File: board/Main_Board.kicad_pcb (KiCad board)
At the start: 2 copper layers, 5 parts, among them U1 Teensy4.1_DEV-16771

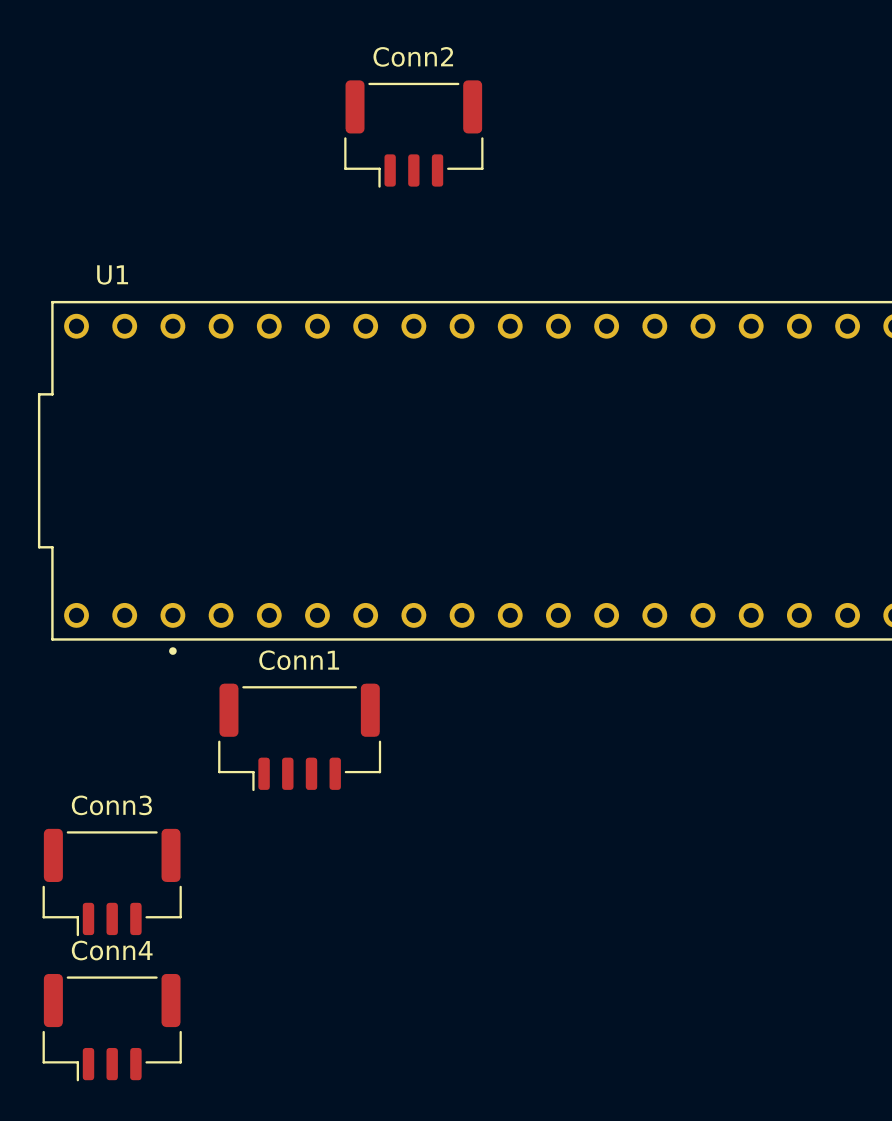
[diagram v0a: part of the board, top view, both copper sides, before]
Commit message: Move Power Indicators
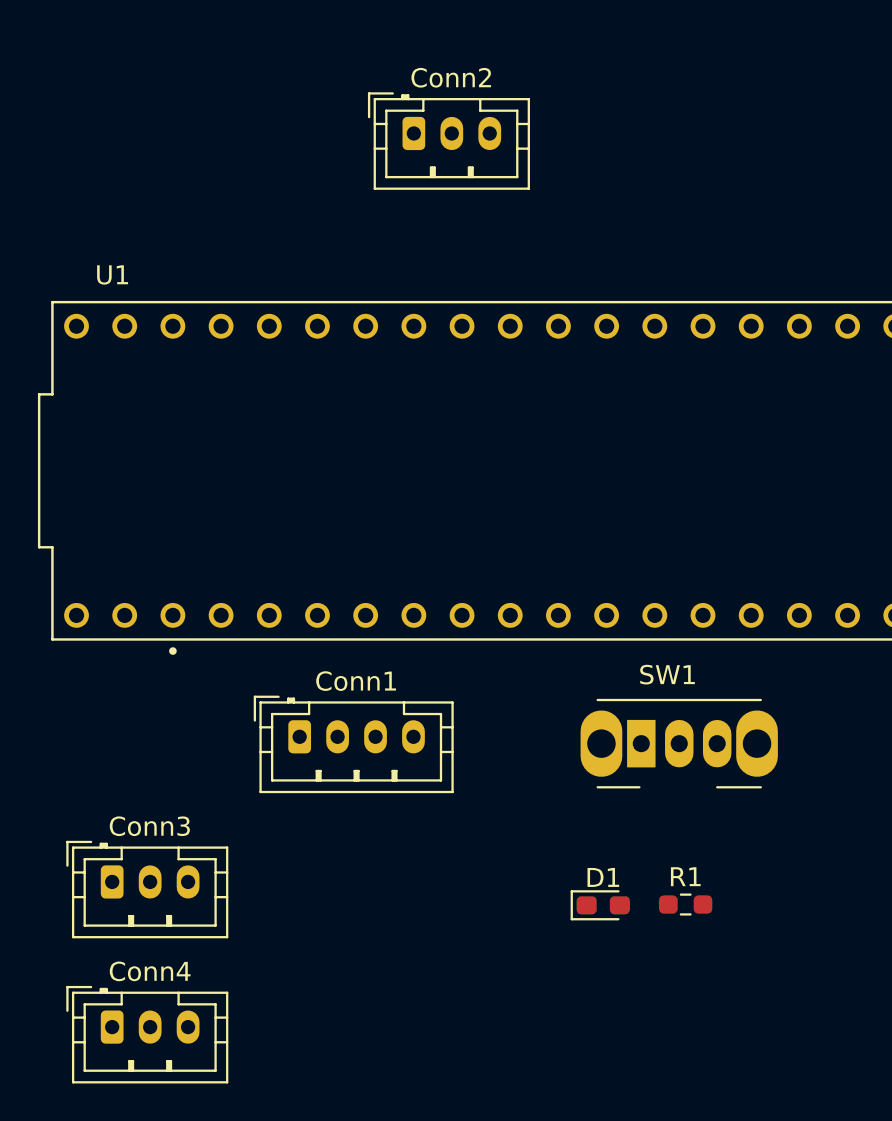
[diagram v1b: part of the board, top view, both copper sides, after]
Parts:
- added D1: LED, LED_SMD:LED_0603_1608Metric_Pad1.05x0.95mm_HandSolder, F.Cu at (144.6, 106.7)
- added R1: 330, Resistor_SMD:R_0603_1608Metric_Pad0.98x0.95mm_HandSolder, F.Cu at (148.9, 106.7)
- added SW1: SW_SPDT, Button_Switch_THT:SW_Slide_SPDT_Angled_CK_OS102011MA1Q, F.Cu at (146.6, 98.2)
- Conn1: footprint Connector_JST:JST_GH_BM04B-GHS-TBT_1x04-1MP_P1.25mm_Vertical -> Connector_JST:JST_PH_B4B-PH-K_1x04_P2.00mm_Vertical
- Conn2, Conn3, Conn4: footprint Connector_JST:JST_GH_BM03B-GHS-TBT_1x03-1MP_P1.25mm_Vertical -> Connector_JST:JST_PH_B3B-PH-K_1x03_P2.00mm_Vertical
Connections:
- U1 pad 19: unconnected-(U1-A5-Pad19) -> Enable

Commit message: Fix Breakout Board
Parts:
- added Conn5: Molex_SL_03, Connector_JST:JST_PH_B3B-PH-K_1x03_P2.00mm_Vertical, F.Cu at (177.9, 68.1)
- moved Conn4 51.8 mm to (145.8, 69.0)
- moved Conn3 51.4 mm to (154.9, 69.1)
- moved D1 45.7 mm to (173.2, 71.1)
- moved R1 41.0 mm to (173.2, 73.7)
- moved SW1 37.6 mm to (122.9, 69.1), turned to 180 degrees
- moved Conn2 29.6 mm to (164.1, 69.1)
- moved Conn1 29.4 mm to (134.7, 69.1)
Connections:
- U1 pad 17: QE1-1 -> AE4
- U1 pad 18: QE1-2 -> QE1-1
- U1 pad 19: Enable -> QE1-2
- U1 pad 20: unconnected-(U1-A6-Pad20) -> Enable
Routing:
- net (no net): track 0.00 -> 168.0 mm
- net AE1: track 0.00 -> 7.13 mm, vias 0 -> 2
- net AE2: track 0.00 -> 3.06 mm
- net Net-(D1-A): track 0.00 -> 2.50 mm

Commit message: Update Mini Arm Board
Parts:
- added Enable: BLUE, LED_SMD:LED_0603_1608Metric_Pad1.05x0.95mm_HandSolder, F.Cu at (116.8, 73.0)
- added R3: 200, Resistor_SMD:R_0603_1608Metric_Pad0.98x0.95mm_HandSolder, F.Cu at (118.7, 73.0)
- Power: renamed from D1; value LED -> GREEN
- moved Conn5 36.1 mm to (141.7, 68.1)
- moved Conn3 5.24 mm to (160.1, 68.1)
- moved Conn2 5.18 mm to (169.2, 68.1)
- moved Conn4 5.14 mm to (150.9, 68.1)
- moved Conn1 4.28 mm to (130.6, 68.1)
- moved R1 3.11 mm to (170.2, 73.0)
- moved Power 2.07 mm to (174.0, 73.0), turned to 180 degrees
- moved OFF 1.94 mm to (123.9, 67.4)
- renumbered SW1 to OFF
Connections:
- net QE1-1 renamed QE1-A
- net QE1-2 renamed QE1-B
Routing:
- net (no net): track 168.0 -> 0.00 mm
- net +3V3: track 0.00 -> 78.0 mm, vias 0 -> 1
- net AE1: track 7.13 -> 29.6 mm, vias 2 -> 0
- net Enable: track 0.00 -> 21.1 mm
- net AE2: track 3.06 -> 23.6 mm
- net AE3: track 0.00 -> 17.3 mm
- net AE4: track 0.00 -> 11.0 mm
- net QE1-A: track 0.00 -> 9.21 mm
- net QE1-B: track 0.00 -> 8.98 mm
- net Net-(D3-A): track 0.00 -> 1.92 mm
- added copper zone on B.Cu, net GND
- added copper zone on F.Cu, net GND
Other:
- board outline added: 64.1 x 30.5 mm
- board text added: "3V3"
- board text added: "GND"
- board text added: "Main Arm Controller Mars Rover Design Team Missouri S&T, 2026 Lucas Boeyink Tyler Hughes"
- board text added: "PWM"
- board text added: "PWM.A"

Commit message: Update Main Board
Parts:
- removed Power: GREEN, LED_SMD:LED_0603_1608Metric_Pad1.05x0.95mm_HandSolder
- removed the R1 at (170.2, 73.0)
- added D1: GREEN, LED_SMD:LED_0603_1608Metric_Pad1.05x0.95mm_HandSolder, F.Cu at (113.5, 67.9)
- added D1: GREEN, LED_SMD:LED_0603_1608Metric_Pad1.05x0.95mm_HandSolder, F.Cu at (92.5, 66.1)
- added H3: MountingHole, MountingHole:MountingHole_4.3mm_M4_ISO14580_Pad_TopBottom, F.Cu at (81.9, 52.7)
- added R1: 330, Resistor_SMD:R_0603_1608Metric_Pad0.98x0.95mm_HandSolder, F.Cu at (96.9, 66.0)
- added R1: 330, Resistor_SMD:R_0603_1608Metric_Pad0.98x0.95mm_HandSolder, F.Cu at (115.6, 67.9)
- moved U1 3.89 mm to (142.2, 84.6)
- moved D3 3.30 mm to (113.5, 72.9)
- moved R3 3.30 mm to (115.4, 72.9)
- moved SW1 2.17 mm to (124.2, 65.2)
- renumbered Enable to D3, OFF to SW1
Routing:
- net +3V3: track 78.0 -> 88.9 mm
- net AE1: track 29.6 -> 34.8 mm
- net AE3: track 17.3 -> 20.8 mm
- net AE4: track 11.0 -> 12.1 mm
- net AE2: track 23.6 -> 24.8 mm
- net Enable: track 21.1 -> 22.1 mm
- net QE1-B: track 8.98 -> 9.61 mm
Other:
- board size 64.1 x 30.5 mm -> 66.7 x 33.7 mm
- board text added: "A PWM"
- board text added: "B PWM"
- board text added: "DATA"
- board text added: "ON"
- board text removed: "PWM.A"

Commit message: Add main board general layout
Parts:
- removed Conn1: Molex_SL_04, Connector_JST:JST_PH_B4B-PH-K_1x04_P2.00mm_Vertical
- removed Conn2, Conn3, Conn4, Conn5: Molex_SL_03, Connector_JST:JST_PH_B3B-PH-K_1x03_P2.00mm_Vertical
- removed the D1 at (113.5, 67.9)
- removed the D1 at (92.5, 66.1)
- removed the R1 at (96.9, 66.0)
- removed the R1 at (115.6, 67.9)
- added C1: 4.7u, Capacitor_SMD:C_0603_1608Metric_Pad1.08x0.95mm_HandSolder, F.Cu at (167.0, 98.4)
- added D1: GREEN, LED_SMD:LED_0603_1608Metric_Pad1.05x0.95mm_HandSolder, F.Cu at (137.1, 68.6)
- added H1: MountingHole, MRDT_Drill_Holes:4_40_Hole, F.Cu at (119.4, 71.9)
- added H2: MountingHole, MRDT_Drill_Holes:4_40_Hole, F.Cu at (172.9, 72.0)
- added H4: MountingHole, MRDT_Drill_Holes:4_40_Hole, F.Cu at (119.4, 98.3)
- added J1: X Axis Encoder, Connector_JST:JST_PH_B4B-PH-K_1x04_P2.00mm_Vertical, F.Cu at (146.6, 69.8)
- added J2: J2 Encoder, Connector_JST:JST_PH_B3B-PH-K_1x03_P2.00mm_Vertical, F.Cu at (161.5, 100.3)
- added J3: J3 Encoder, Connector_JST:JST_PH_B3B-PH-K_1x03_P2.00mm_Vertical, F.Cu at (151.3, 100.3)
- added J4: J4 Encoder, Connector_JST:JST_PH_B3B-PH-K_1x03_P2.00mm_Vertical, F.Cu at (141.2, 100.3)
- added J5: Pitch Encoder, Connector_JST:JST_PH_B3B-PH-K_1x03_P2.00mm_Vertical, F.Cu at (130.8, 100.3)
- added J6: I2C Bus, Connector_JST:JST_PH_B2B-PH-K_1x02_P2.00mm_Vertical, F.Cu at (161.3, 69.8)
- added R1: 330, Resistor_SMD:R_0603_1608Metric_Pad0.98x0.95mm_HandSolder, F.Cu at (137.9, 71.4)
- added R2: 200, Resistor_SMD:R_0603_1608Metric_Pad0.98x0.95mm_HandSolder, F.Cu at (141.8, 71.5)
- added R4: 4.7k, Resistor_SMD:R_0603_1608Metric_Pad0.98x0.95mm_HandSolder, F.Cu at (157.5, 71.1)
- H3: footprint MountingHole:MountingHole_4.3mm_M4_ISO14580_Pad_TopBottom -> MRDT_Drill_Holes:4_40_Hole
- R3: value 200 -> 4.7k
- SW1: value SW_SPDT -> Enable Switch
- moved H3 101.8 mm to (172.9, 98.3)
- moved R3 43.6 mm to (159.0, 74.3), turned to 0 degrees
- moved D3 27.6 mm to (140.8, 68.6), turned to 0 degrees
- moved SW1 8.23 mm to (131.0, 69.8)
- moved U1 3.84 mm to (146.1, 85.1)
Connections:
- R3 pad 1: Net-(D3-A) -> +3V3
- R3 pad 2: Enable -> SDA
- U1 pad 18: QE1-A -> SDA
- U1 pad 19: QE1-B -> SCL
- U1 pad 21: unconnected-(U1-A7-Pad21) -> QE1-A
- U1 pad 22: unconnected-(U1-A8-Pad22) -> QE1-B
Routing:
- net +3V3: track 88.9 -> 46.4 mm, vias 1 -> 3
- net AE1: track 34.8 -> 0.00 mm
- net SDA: track 0.00 -> 30.0 mm, vias 0 -> 1
- net SCL: track 0.00 -> 30.0 mm, vias 0 -> 2
- net AE2: track 24.8 -> 0.00 mm
- net AE3: track 20.8 -> 0.00 mm
- net QE1-B: track 9.61 -> 29.3 mm, vias 0 -> 2
- net QE1-A: track 9.39 -> 25.2 mm, vias 0 -> 2
- net AE4: track 12.1 -> 0.00 mm
- net Enable: track 22.1 -> 20.7 mm
- removed copper zone on B.Cu, net GND
- removed copper zone on F.Cu, net GND
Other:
- board size 66.7 x 33.7 mm -> 61.6 x 34.5 mm
- board text removed: "3V3"
- board text removed: "A PWM"
- board text removed: "B PWM"
- board text removed: "DATA"
- board text removed: "GND"
- board text removed: "Main Arm Controller Mars Rover Design Team Missouri S&T, 2026 Lucas Boeyink Tyler Hughes"
- board text removed: "ON"
- board text removed: "PWM"

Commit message: Complete main board pre-review
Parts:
- I2C Bus: renamed from J6
- J2 Encoder: renamed from J2
- J3 Encoder: renamed from J3
- J4 Encoder: renamed from J4
- Pitch Encoder: renamed from J5
- X Axis Encoder: renamed from J1
- moved R3 0.63 mm to (158.4, 74.3)
- moved H2 0.46 mm to (172.8, 71.5)
- moved H1 0.38 mm to (119.4, 71.5)
- moved H3 0.26 mm to (172.8, 98.6)
- moved H4 0.25 mm to (119.4, 98.6)
- renumbered SW1 to ENABLE
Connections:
- U1 pad 14: AE1 -> unconnected-(U1-A0-Pad14)
- U1 pad 15: AE2 -> unconnected-(U1-A1-Pad15)
- U1 pad 16: AE3 -> unconnected-(U1-A2-Pad16)
- U1 pad 17: AE4 -> unconnected-(U1-A3-Pad17)
- U1 pad 24: unconnected-(U1-A10-Pad24) -> AE4
- U1 pad 25: unconnected-(U1-A11-Pad25) -> AE3
- U1 pad 26: unconnected-(U1-A12-Pad26) -> AE2
- U1 pad 27: unconnected-(U1-A13-Pad27) -> AE1
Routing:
- net +3V3: track 46.4 -> 111.3 mm, vias 3 -> 8
- net AE4: track 0.00 -> 31.8 mm, vias 0 -> 2
- net AE3: track 0.00 -> 25.1 mm, vias 0 -> 2
- net AE2: track 0.00 -> 17.3 mm, vias 0 -> 2
- net AE1: track 0.00 -> 10.0 mm, vias 0 -> 2
- net SCL: track 30.0 -> 32.4 mm
- net Enable: track 20.7 -> 19.1 mm
- net QE1-B: track 29.3 -> 30.5 mm
- net QE1-A: track 25.2 -> 26.1 mm
- added copper zone on B.Cu, net GND
- added copper zone on F.Cu, net GND
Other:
- board size 61.6 x 34.5 mm -> 61.6 x 35.2 mm
- board text added: "3V3"
- board text added: "A"
- board text added: "B"
- board text added: "DISABLE"
- board text added: "ENABLE"
- board text added: "GND"
- board text added: "Mini Arm Controller Main Board Mars Rover Design Team Missouri S&T, 2026 Lucas Boeyink, Tyler Hughes"
- board text added: "OUT"
- board text added: "POWER"
- board text added: "SCL"
- board text added: "SDA"

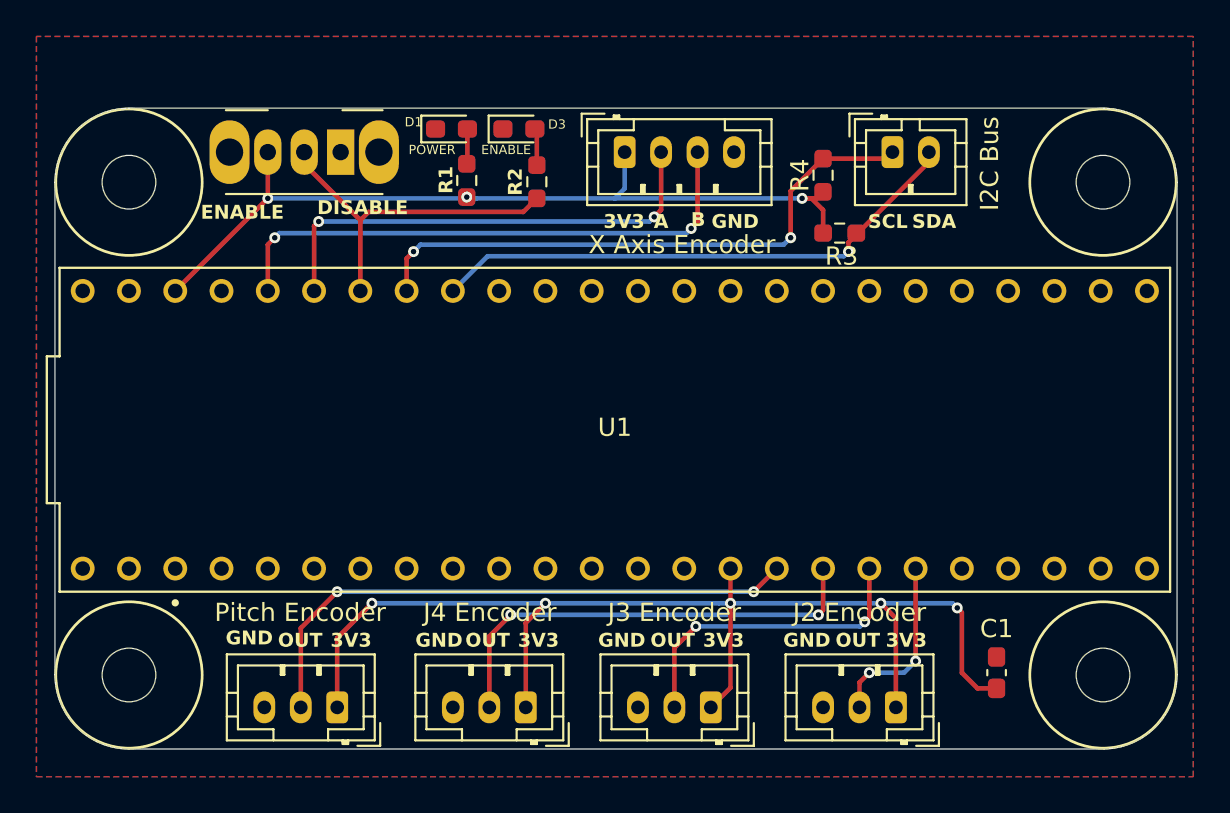
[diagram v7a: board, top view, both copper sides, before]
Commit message: Adjust main board size
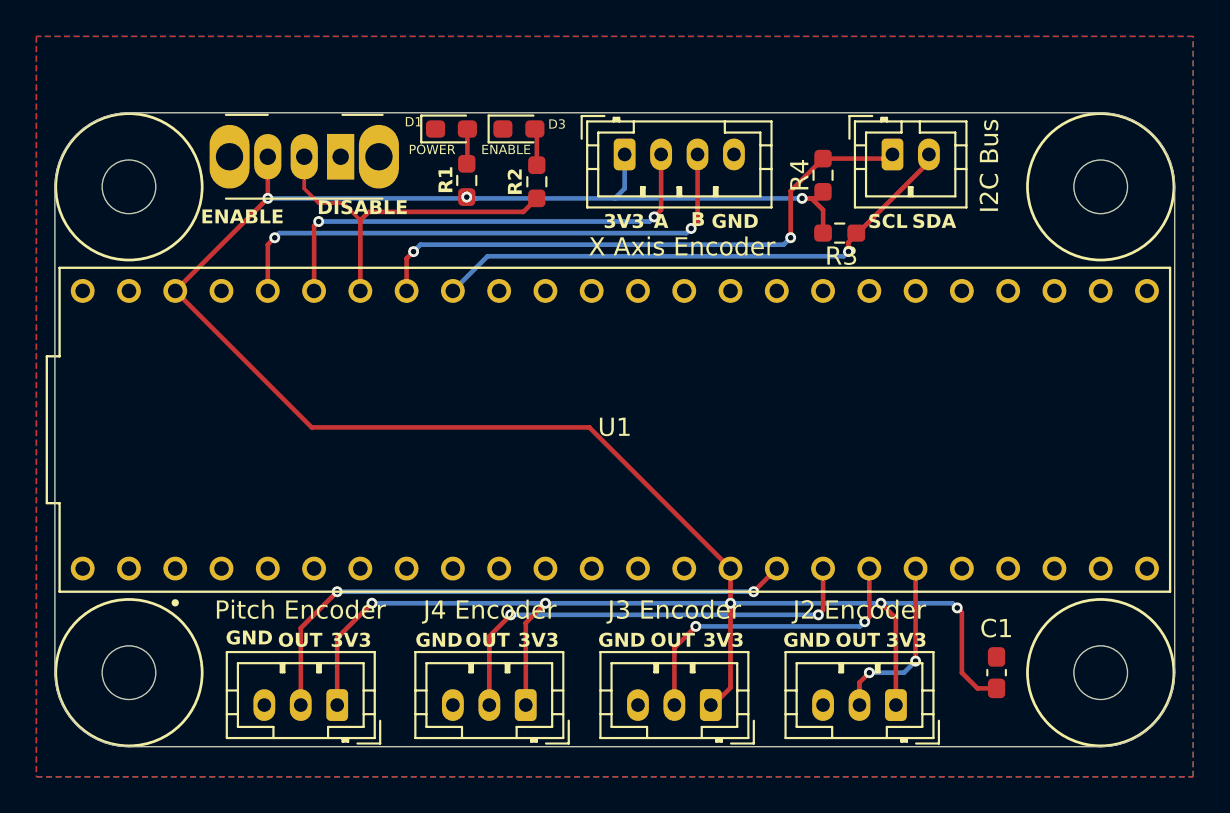
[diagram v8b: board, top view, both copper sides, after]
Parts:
- removed H1, H4: MountingHole, MRDT_Drill_Holes:4_40_Hole
- added H2: MountingHole, MRDT_Drill_Holes:4_40_Hole, F.Cu at (119.4, 71.8)
- added H3: MountingHole, MRDT_Drill_Holes:4_40_Hole, F.Cu at (119.4, 98.4)
- moved H2 0.28 mm to (172.7, 71.8)
- moved ENABLE 0.25 mm to (131.0, 70.1)
- moved H3 0.18 mm to (172.7, 98.4)
- moved I2C Bus 0.13 mm to (161.3, 70.0)
- moved X Axis Encoder 0.13 mm to (146.6, 70.0)
- moved J2 Encoder 0.13 mm to (161.5, 100.2)
- moved J3 Encoder 0.13 mm to (151.3, 100.2)
- moved J4 Encoder 0.13 mm to (141.2, 100.2)
- moved Pitch Encoder 0.13 mm to (130.8, 100.2)
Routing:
- net +3V3: track 111.3 -> 147.8 mm
- net Enable: track 19.1 -> 20.3 mm
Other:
- board size 61.6 x 35.2 mm -> 61.5 x 34.8 mm
